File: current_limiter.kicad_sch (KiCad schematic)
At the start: 31 parts, among them J1 VIN, J2 VOUT, Q1 BSC040N10NS5, Q2 BC849, Q3 BC858, U1 TLV1805QDBVRQ1, U2 INA181A2IDBVR, U3 LM8261

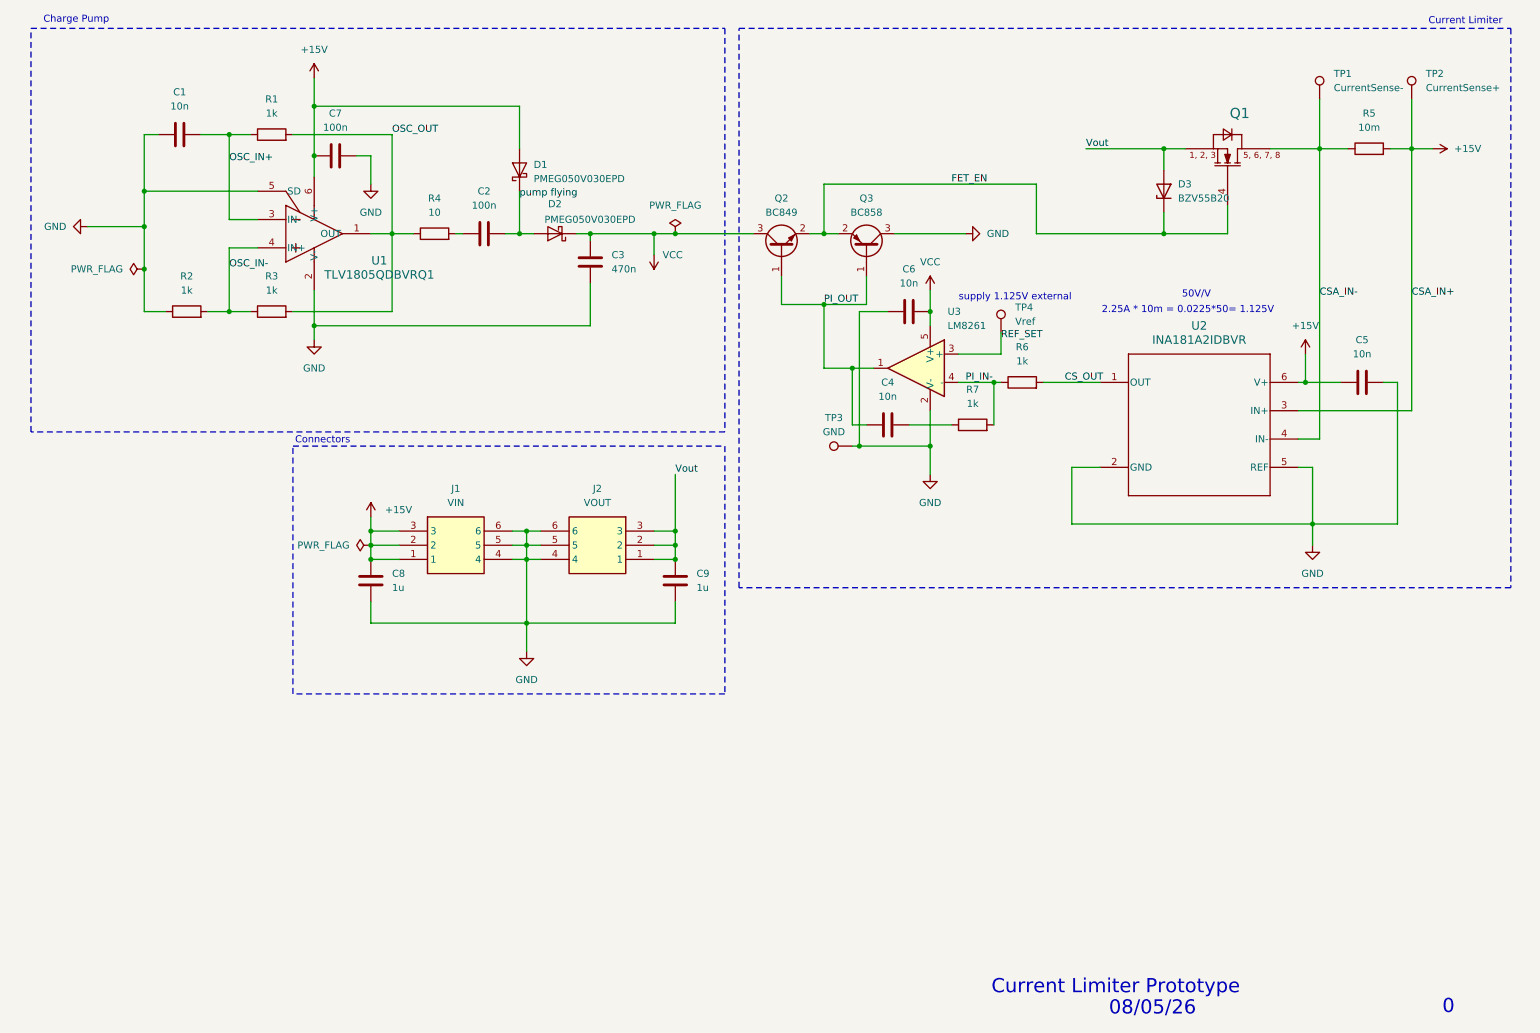
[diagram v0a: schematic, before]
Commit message: version 2: changed opamp & diodes to more responsible components, changed reference voltage
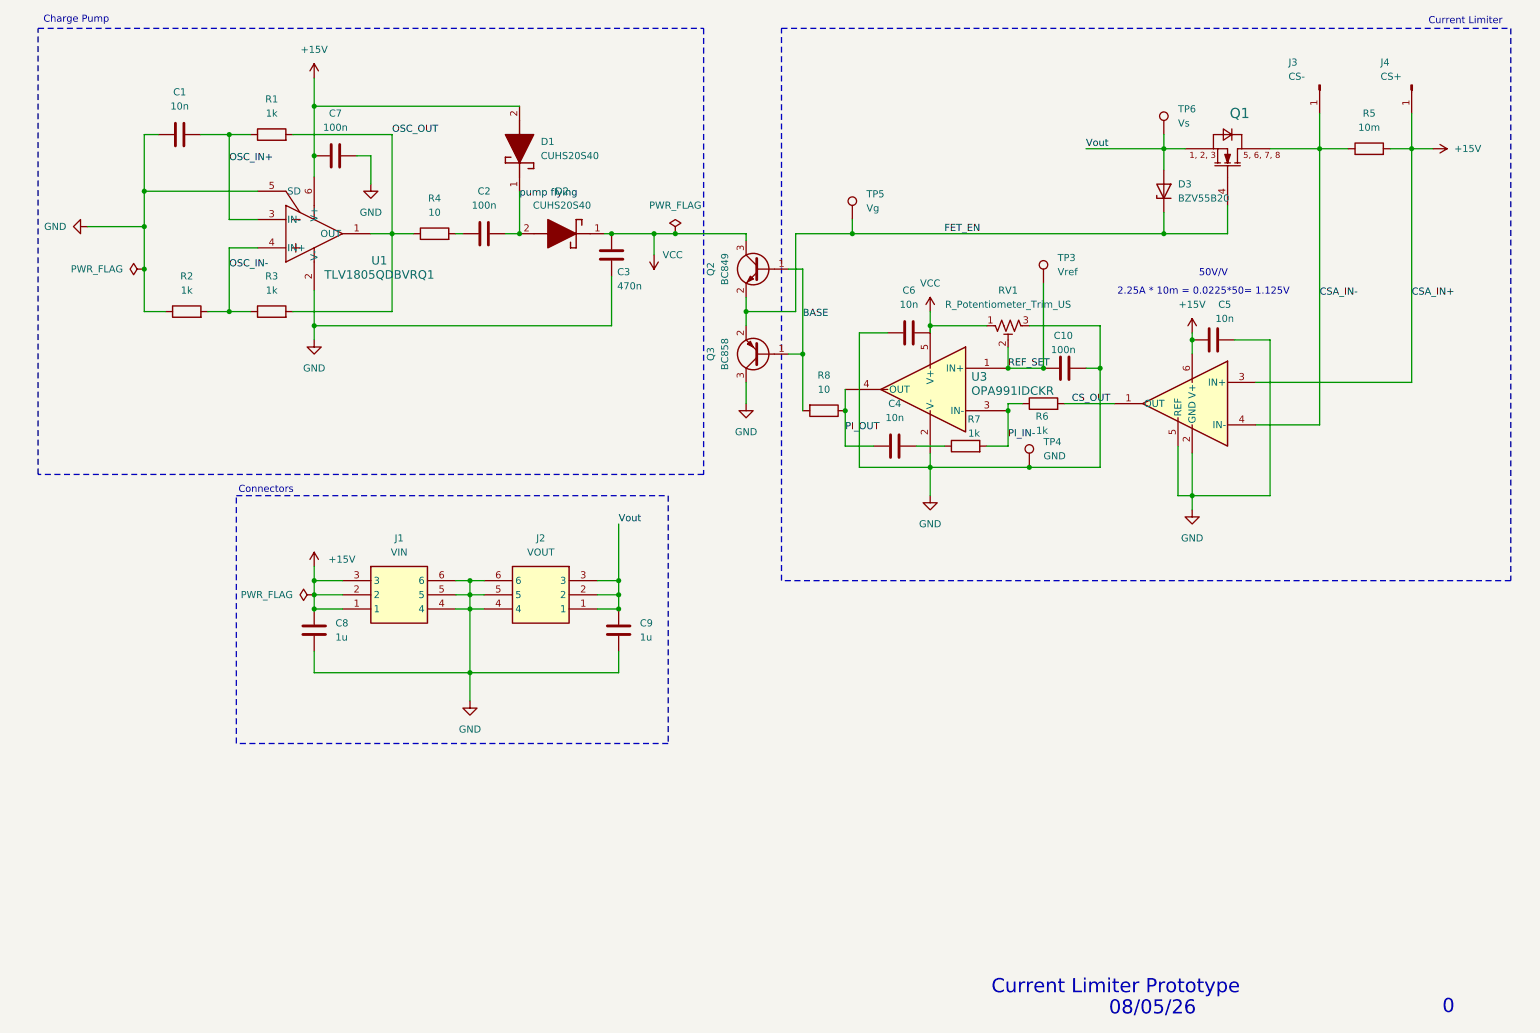
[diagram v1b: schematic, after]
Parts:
- removed D1, D2: PMEG050V030EPD, Package_TO_SOT_SMD:Nexperia_CFP15_SOT-1289, symbol Diode:PMEG050V030EPD
- removed TP1: CurrentSense-, TestPoint:TestPoint_THTPad_D2.0mm_Drill1.0mm, symbol Connector:TestPoint
- removed TP2: CurrentSense+, TestPoint:TestPoint_THTPad_D2.0mm_Drill1.0mm, symbol Connector:TestPoint
- removed U2: INA181A2IDBVR, Current_Limiter_Stuff:DBV0006A_L, symbol Current_Limiter_Stuff:INA181A2IDBVR
- removed U3: LM8261, Package_TO_SOT_SMD:SOT-23-5, symbol Amplifier_Operational:LM8261
- added C10: 100n, Capacitor_SMD:C_0805_2012Metric, symbol Device:C
- added D1, D2: CUHS20S40, Current_Limiter_Stuff:CUHS20S40, symbol Current-limiter-stuff:CUHS20S40
- added J3: CS-, Connector_PinHeader_1.27mm:PinHeader_1x01_P1.27mm_Vertical, symbol Connector:Conn_01x01_Pin
- added J4: CS+, Connector_PinHeader_1.27mm:PinHeader_1x01_P1.27mm_Vertical, symbol Connector:Conn_01x01_Pin
- added R8: 10, Resistor_SMD:R_0402_1005Metric, symbol Device:R
- added RV1: R_Potentiometer_Trim_US, Potentiometer_THT:Potentiometer_Runtron_RM-063_Horizontal, symbol Device:R_Potentiometer_Trim_US
- added TP5: Vg, TestPoint:TestPoint_Pad_D2.0mm, symbol Connector:TestPoint
- added TP6: Vs, TestPoint:TestPoint_Pad_D2.0mm, symbol Connector:TestPoint
- added U2: INA181A2IDBVR, Current_Limiter_Stuff:DBV0006A_L, symbol current-limiter-stuff:INA181A2IDBVR
- added U3: OPA991IDCKR, Current_Limiter_Stuff:SC_91IDCKR_TEX, symbol Current-limiter-stuff:OPA991IDCKR
- C4: footprint Capacitor_SMD:C_0402_1005Metric -> Capacitor_SMD:C_0805_2012Metric
- R6, R7: footprint Resistor_SMD:R_0402_1005Metric -> Capacitor_SMD:C_0805_2012Metric
- TP3: value GND -> Vref; footprint TestPoint:TestPoint_THTPad_D2.0mm_Drill1.0mm -> TestPoint:TestPoint_Pad_D2.0mm
- TP4: value Vref -> GND; footprint TestPoint:TestPoint_THTPad_D2.0mm_Drill1.0mm -> TestPoint:TestPoint_Pad_D2.0mm
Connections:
- net +15V: now also D1.2 (A), J4.1 (Pin_1), U2.3 (IN+), U2.6 (V+)
- net CSA_IN-: now also J3.1 (Pin_1), U2.4 (IN-)
- net CS_OUT: now also U2.1 (OUT)
- net FET_EN: now also TP5.1
- net GND: now also TP4.1, C10.2, RV1.3, U2.2 (GND), U2.5 (REF), U3.2 (V-); no longer TP3.1
- net PI_IN-: now also U3.3 (IN-)
- net PI_OUT: now also R8.1, U3.4 (OUT); no longer Q2.1 (B), Q3.1 (B)
- net REF_SET: now also TP3.1, C10.1, RV1.2, U3.1 (IN+); no longer TP4.1
- net VCC: now also D2.1 (K), RV1.1, U3.5 (V+)
- net Vout: now also TP6.1
- net pump flying: now also D1.1 (K), D2.2 (A)
- new net BASE: Q2.1 (B), Q3.1 (B), R8.2
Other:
- note removed: "supply 1.125V external"
- moved on the sheet: C3, C4, C5, C6, C8, C9, J1, J2, Q2, Q3, R6, R7

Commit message: minor updates, moved caps around + added resistor for current limiting
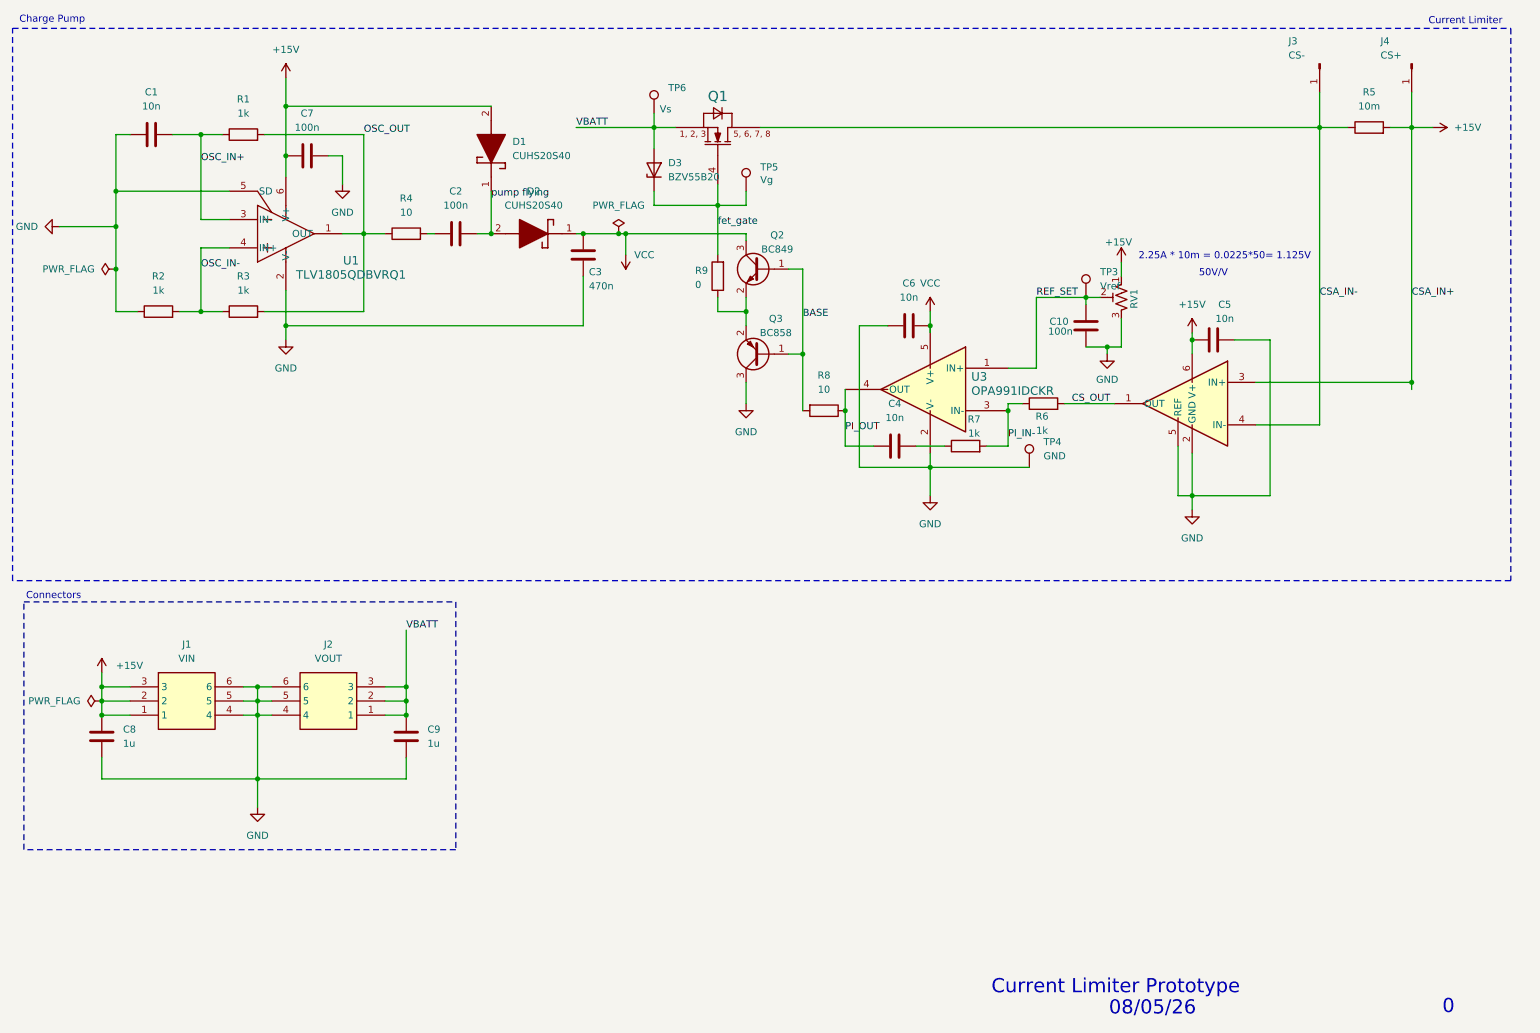
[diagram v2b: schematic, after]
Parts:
- added R9: 0, Resistor_SMD:R_0805_2012Metric, symbol Device:R
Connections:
- net +15V: now also RV1.1
- net GND: now also C10.1; no longer C10.2
- net REF_SET: now also C10.2; no longer C10.1
- net VCC: no longer RV1.1
- net FET_EN renamed fet_gate
- net fet_gate: now also R9.2; no longer Q2.2 (E), Q3.2 (E)
- net Vout renamed VBATT
- new net: Q2.2 (E), Q3.2 (E), R9.1
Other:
- moved on the sheet: C1, C10, C2, C3, C6, C7, C8, C9, D1, D2, D3, J1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

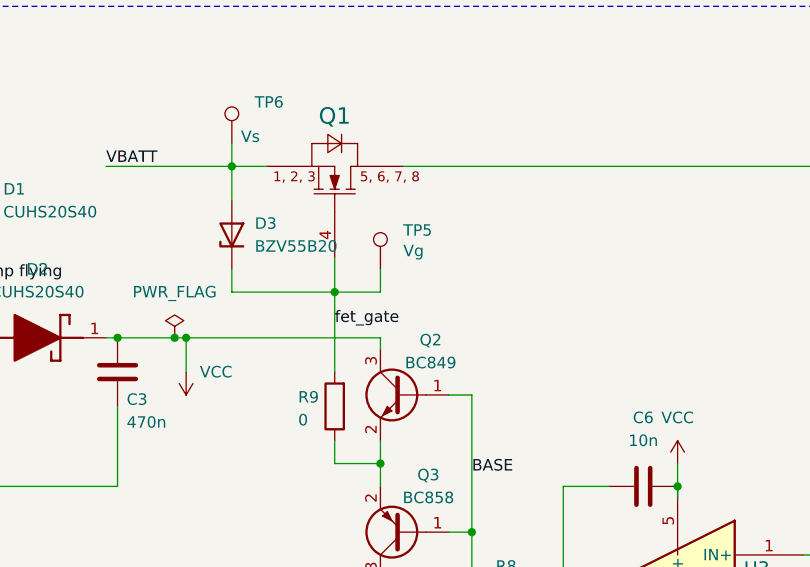
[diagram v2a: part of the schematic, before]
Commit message: minor updates, added second zener to cap negative Vgs and DNP diode for potential minimum opamp output
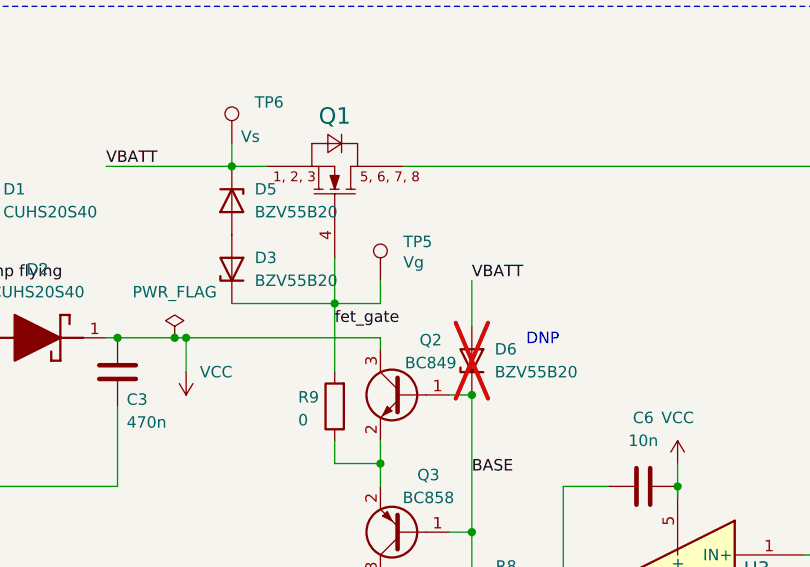
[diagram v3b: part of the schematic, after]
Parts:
- added D5, D6: BZV55B20, Diode_SMD:D_MiniMELF, symbol Diode:BZV55B20
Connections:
- net BASE: now also D6.1 (K)
- net VBATT: now also D5.1 (K), D6.2 (A); no longer D3.2 (A)
- new net: D3.2 (A), D5.2 (A)
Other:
- note added: "DNP"
- moved on the sheet: D3, TP5
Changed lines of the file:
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@@
 		)
 	)
+	(text "DNP\n"
+		(exclude_from_sim no)
+		(at 162.814 54.864 0)
+		(effects
+			(font
+				(size 1.27 1.27)
+			)
+		)
+	)
 	(text "Charge Pump\n"
 		(exclude_from_sim no)
@@
 	)
 	(junction
+		(at 154.94 60.96)
+		(diameter 0)
+		(color 0 0 0 0)
+	)
+	(junction
 		(at 144.78 68.58)
 		(diameter 0)
@@
 	)
 	(junction
+		(at 139.7 50.8)
+		(diameter 0)
+		(color 0 0 0 0)
+	)
+	(junction
 		(at 57.15 140.97)
 		(diameter 0)
@@
 	)
 	(junction
-		(at 139.7 49.53)
-		(diameter 0)
-		(color 0 0 0 0)
-	)
-	(junction
 		(at 162.56 86.36)
 		(diameter 0)
@@
 	(wire
 		(pts
-			(xy 128.27 49.53) (xy 139.7 49.53)
-		)
-		(stroke
-			(width 0)
-			(type default)
-		)
-	)
-	(wire
-		(pts
 			(xy 205.74 66.04) (xy 205.74 67.31)
 		)
@@
 	(wire
 		(pts
-			(xy 128.27 33.02) (xy 128.27 35.56)
-		)
-		(stroke
-			(width 0)
-			(type default)
-		)
-	)
-	(wire
-		(pts
 			(xy 222.25 92.71) (xy 222.25 101.6)
 		)
@@
 	(wire
 		(pts
+			(xy 154.94 48.26) (xy 154.94 53.34)
+		)
+		(stroke
+			(width 0)
+			(type default)
+		)
+	)
+	(wire
+		(pts
 			(xy 165.1 71.12) (xy 165.1 96.52)
 		)
@@
 	(wire
 		(pts
-			(xy 128.27 35.56) (xy 128.27 39.37)
-		)
-		(stroke
-			(width 0)
-			(type default)
-		)
-	)
-	(wire
-		(pts
 			(xy 196.85 66.04) (xy 196.85 78.74)
 		)
@@
 	(wire
 		(pts
-			(xy 144.78 46.99) (xy 144.78 49.53)
+			(xy 144.78 48.26) (xy 144.78 50.8)
 		)
 		(stroke
@@
 	(wire
 		(pts
+			(xy 139.7 50.8) (xy 139.7 58.42)
+		)
+		(stroke
+			(width 0)
+			(type default)
+		)
+	)
+	(wire
+		(pts
 			(xy 208.28 66.04) (xy 205.74 66.04)
 		)
@@
 	(wire
 		(pts
+			(xy 128.27 50.8) (xy 139.7 50.8)
+		)
+		(stroke
+			(width 0)
+			(type default)
+		)
+	)
+	(wire
+		(pts
 			(xy 62.23 31.75) (xy 99.06 31.75)
 		)
@@
 	(wire
 		(pts
-			(xy 139.7 49.53) (xy 144.78 49.53)
+			(xy 139.7 50.8) (xy 144.78 50.8)
 		)
 		(stroke
@@
 	(wire
 		(pts
+			(xy 128.27 33.02) (xy 128.27 35.56)
+		)
+		(stroke
+			(width 0)
+			(type default)
+		)
+	)
+	(wire
+		(pts
 			(xy 57.15 152.4) (xy 57.15 157.48)
 		)
@@
 	(wire
 		(pts
-			(xy 139.7 49.53) (xy 139.7 58.42)
-		)
-		(stroke
-			(width 0)
-			(type default)
-		)
-	)
-	(wire
-		(pts
 			(xy 83.82 125.73) (xy 83.82 135.89)
 		)
@@
 	(wire
 		(pts
-			(xy 139.7 45.72) (xy 139.7 49.53)
+			(xy 139.7 45.72) (xy 139.7 50.8)
 		)
 		(stroke
@@
 		)
 	)
-	(wire
-		(pts
-			(xy 128.27 46.99) (xy 128.27 49.53)
-		)
-		(stroke
-			(width 0)
-			(type default)
-		)
-	)
 	(label "fet_gate"
 		(at 139.7 53.34 0)
@@
 		)
 	)
+	(label "VBATT"
+		(at 154.94 48.26 0)
+		(effects
+			(font
+				(size 1.27 1.27)
+			)
+			(justify left bottom)
+		)
+	)
 	(label "OSC_IN-"
 		(at 46.99 60.96 0)
@@
 	)
 	(symbol
+		(lib_id "Diode:BZV55B20")
+		(at 128.27 39.37 270)
+		(unit 1)
+		(body_style 1)
+		(exclude_from_sim no)
+		(in_bom yes)
+		(on_board yes)
+		(in_pos_files yes)
+		(dnp no)
+		(fields_autoplaced yes)
+		(property "Reference" "D5"
+			(at 130.81 38.0999 90)
+			(show_name no)
+			(do_not_autoplace no)
+			(effects
+				(font
+					(size 1.27 1.27)
+				)
+				(justify left)
+			)
+		)
+		(property "Value" "BZV55B20"
+			(at 130.81 40.6399 90)
+			(show_name no)
+			(do_not_autoplace no)
+			(effects
+				(font
+					(size 1.27 1.27)
+				)
+				(justify left)
+			)
+		)
+		(property "Footprint" "Diode_SMD:D_MiniMELF"
+			(at 123.825 39.37 0)
+			(hide yes)
+			(show_name no)
+			(do_not_autoplace no)
+			(effects
+				(font
+					(size 1.27 1.27)
+				)
+			)
+		)
+		(property "Datasheet" "https://assets.nexperia.com/documents/data-sheet/BZV55_SER.pdf"
+			(at 128.27 39.37 0)
+			(hide yes)
+			(show_name no)
+			(do_not_autoplace no)
+			(effects
+				(font
+					(size 1.27 1.27)
+				)
+			)
+		)
+		(property "Description" "20V, 500mW, 2%, Zener diode, MiniMELF"
+			(at 128.27 39.37 0)
+			(hide yes)
+			(show_name no)
+			(do_not_autoplace no)
+			(effects
+				(font
+					(size 1.27 1.27)
+				)
+			)
+		)
+		(pin "1"
+		)
+		(pin "2"
+		)
+		(instances
+			(project "current_limiter"
+				(path "/9cad53dd-e6ec-4945-b0cd-3a61fa1e6914"
+					(reference "D5")
+					(unit 1)
+				)
+			)
+		)
+	)
+	(symbol
 		(lib_id "Device:R")
 		(at 139.7 62.23 180)
@@
 	(symbol
 		(lib_id "Diode:BZV55B20")
-		(at 128.27 43.18 90)
+		(at 128.27 46.99 90)
 		(unit 1)
 		(body_style 1)
@@
 		(fields_autoplaced yes)
 		(property "Reference" "D3"
-			(at 130.81 41.9099 90)
+			(at 130.81 45.7199 90)
 			(show_name no)
 			(do_not_autoplace no)
@@
 		)
 		(property "Value" "BZV55B20"
-			(at 130.81 44.4499 90)
+			(at 130.81 48.2599 90)
 			(show_name no)
 			(do_not_autoplace no)
@@
 		)
 		(property "Footprint" "Diode_SMD:D_MiniMELF"
-			(at 132.715 43.18 0)
+			(at 132.715 46.99 0)
 			(hide yes)
 			(show_name no)
@@
 		)
 		(property "Datasheet" "https://assets.nexperia.com/documents/data-sheet/BZV55_SER.pdf"
-			(at 128.27 43.18 0)
+			(at 128.27 46.99 0)
 			(hide yes)
 			(show_name no)
@@
 		)
 		(property "Description" "20V, 500mW, 2%, Zener diode, MiniMELF"
-			(at 128.27 43.18 0)
+			(at 128.27 46.99 0)
 			(hide yes)
 			(show_name no)
@@
 	)
 	(symbol
+		(lib_id "Diode:BZV55B20")
+		(at 154.94 57.15 90)
+		(unit 1)
+		(body_style 1)
+		(exclude_from_sim no)
+		(in_bom yes)
+		(on_board yes)
+		(in_pos_files yes)
+		(dnp yes)
+		(fields_autoplaced yes)
+		(property "Reference" "D6"
+			(at 157.48 55.8799 90)
+			(show_name no)
+			(do_not_autoplace no)
+			(effects
+				(font
+					(size 1.27 1.27)
+				)
+				(justify right)
+			)
+		)
+		(property "Value" "BZV55B20"
+			(at 157.48 58.4199 90)
+			(show_name no)
+			(do_not_autoplace no)
+			(effects
+				(font
+					(size 1.27 1.27)
+				)
+				(justify right)
+			)
+		)
+		(property "Footprint" "Diode_SMD:D_MiniMELF"
+			(at 159.385 57.15 0)
+			(hide yes)
+			(show_name no)
+			(do_not_autoplace no)
+			(effects
+				(font
+					(size 1.27 1.27)
+				)
+			)
+		)
+		(property "Datasheet" "https://assets.nexperia.com/documents/data-sheet/BZV55_SER.pdf"
+			(at 154.94 57.15 0)
+			(hide yes)
+			(show_name no)
+			(do_not_autoplace no)
+			(effects
+				(font
+					(size 1.27 1.27)
+				)
+			)
+		)
+		(property "Description" "20V, 500mW, 2%, Zener diode, MiniMELF"
+			(at 154.94 57.15 0)
+			(hide yes)
+			(show_name no)
+			(do_not_autoplace no)
+			(effects
+				(font
+					(size 1.27 1.27)
+				)
+			)
+		)
+		(pin "1"
+		)
+		(pin "2"
+		)
+		(instances
+			(project "current_limiter"
+				(path "/9cad53dd-e6ec-4945-b0cd-3a61fa1e6914"
+					(reference "D6")
+					(unit 1)
+				)
+			)
+		)
+	)
+	(symbol
 		(lib_id "Device:C")
 		(at 115.57 58.42 180)
@@
 	(symbol
 		(lib_id "Connector:TestPoint")
-		(at 144.78 46.99 0)
+		(at 144.78 48.26 0)
 		(unit 1)
 		(body_style 1)
@@
 		(dnp no)
 		(property "Reference" "TP5"
-			(at 147.32 42.672 0)
+			(at 147.32 43.942 0)
 			(show_name no)
 			(do_not_autoplace no)
@@
 		)
 		(property "Value" "Vg"
-			(at 147.32 44.9579 0)
+			(at 147.32 46.2279 0)
 			(show_name no)
 			(do_not_autoplace no)
@@
 		)
 		(property "Footprint" "TestPoint:TestPoint_Pad_D2.0mm"
-			(at 149.86 46.99 0)
+			(at 149.86 48.26 0)
 			(hide yes)
 			(show_name no)
@@
 		)
 		(property "Datasheet" ""
-			(at 149.86 46.99 0)
+			(at 149.86 48.26 0)
 			(hide yes)
 			(show_name no)
@@
 		)
 		(property "Description" "test point"
-			(at 144.78 46.99 0)
+			(at 144.78 48.26 0)
 			(hide yes)
 			(show_name no)
